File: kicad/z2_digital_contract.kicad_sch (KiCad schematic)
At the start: 0 parts

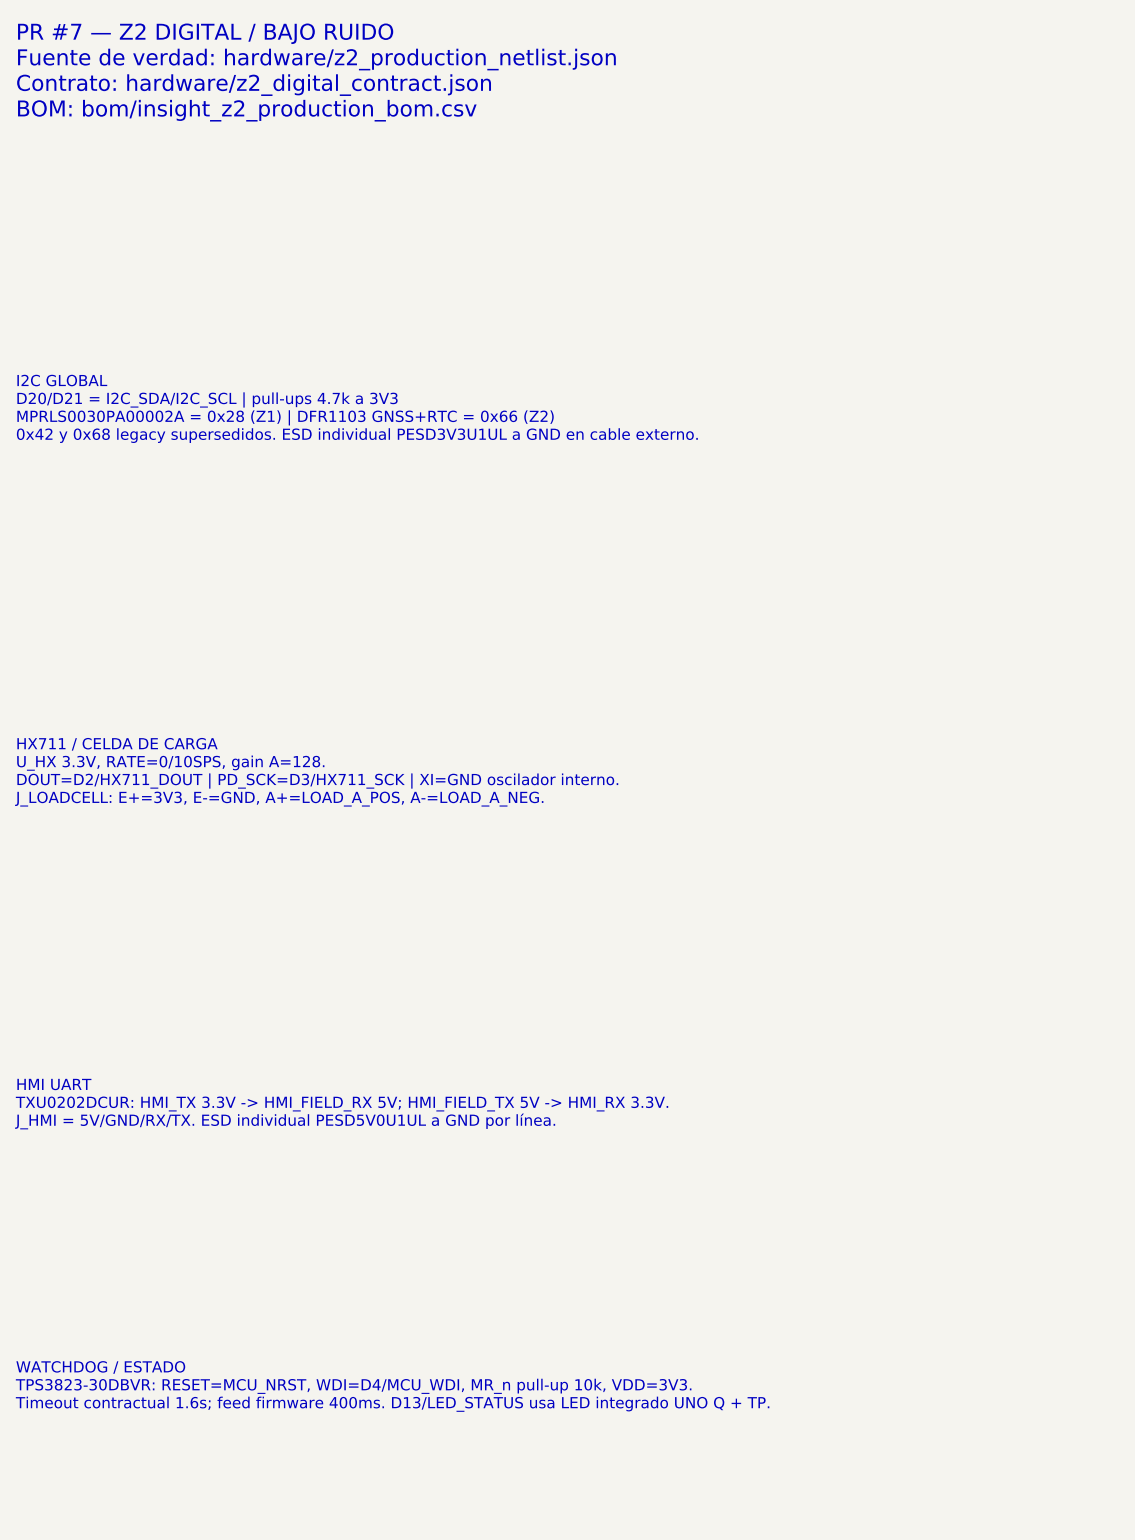
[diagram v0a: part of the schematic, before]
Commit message: potencia: congelar arquitectura Fase 3 y frontera UNO Q (#9)
Congela el power tree del shield sobre 12V→VIN UNO Q, separa rails locales 5V/3V3, selecciona eFuse/buck/LDO, formaliza GitHub oficial Arduino como fuente primaria y mantiene Z1/Z2/compliance coherentes.
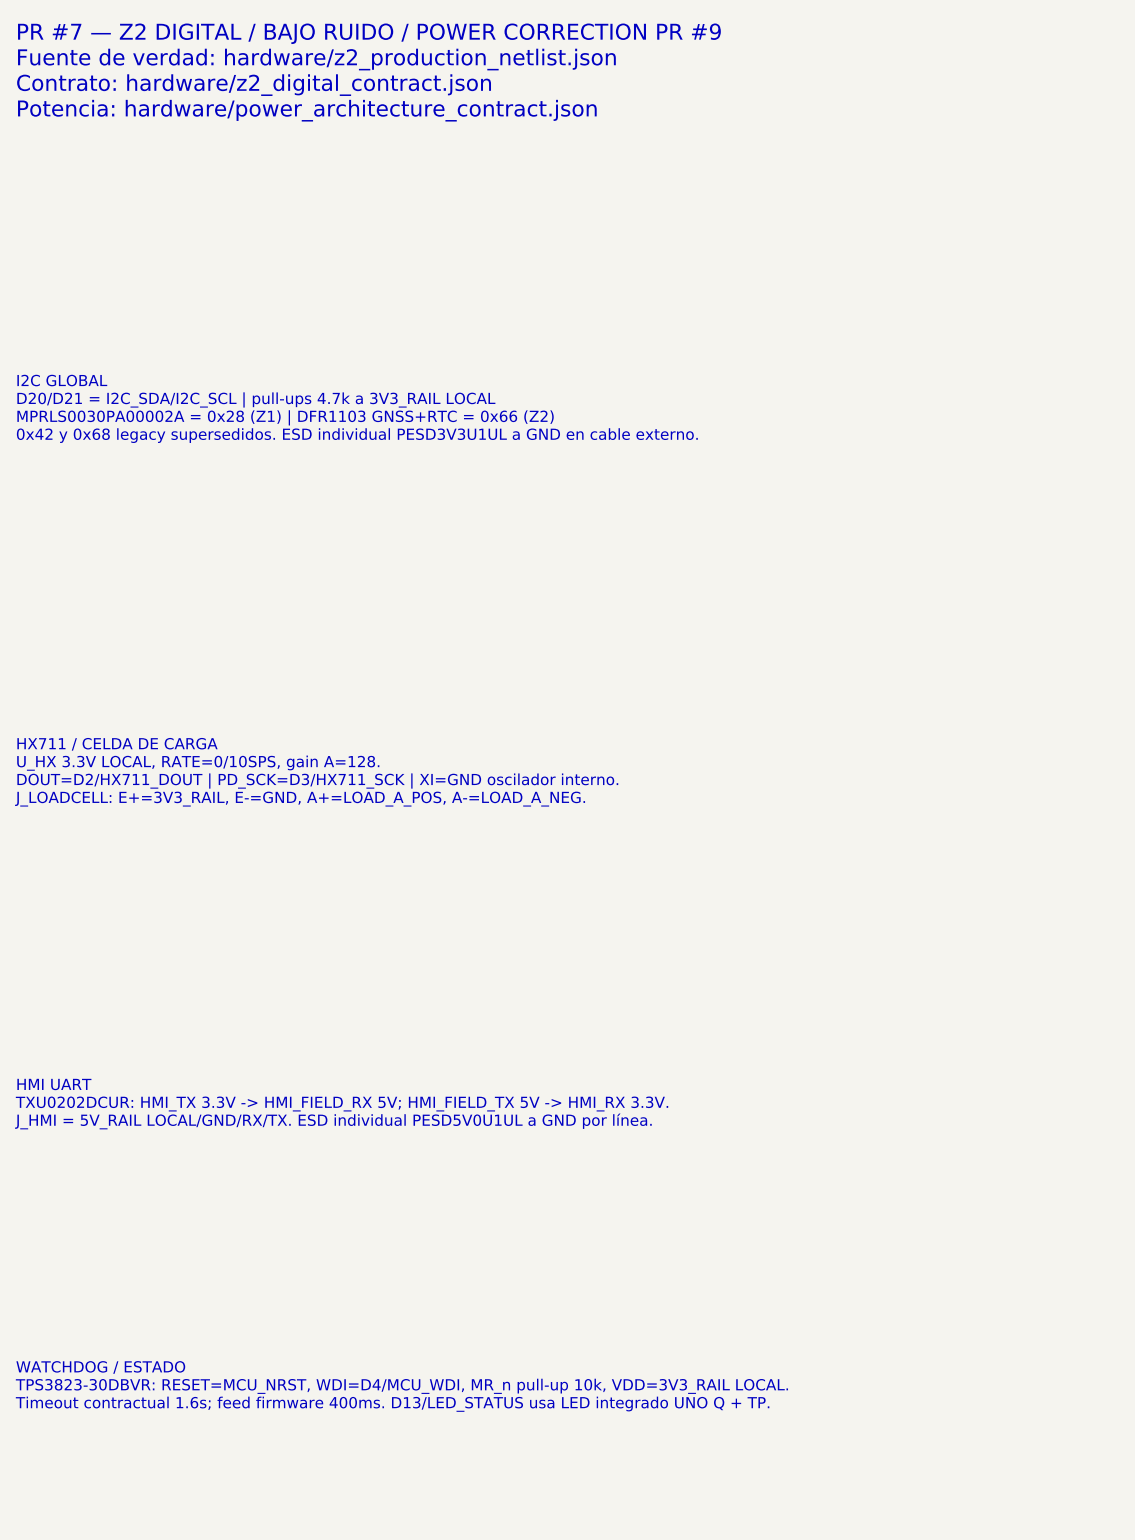
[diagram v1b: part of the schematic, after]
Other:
- note added: "HMI UART TXU0202DCUR: HMI_TX 3.3V -> HMI_FIELD_RX 5V; HMI_FIELD_TX 5V -> HMI_RX 3.3V. J_HMI = 5V_RAIL LOCAL/GND/RX/TX. ESD individual PESD5V0U1UL a GND por línea."
- note added: "HX711 / CELDA DE CARGA U_HX 3.3V LOCAL, RATE=0/10SPS, gain A=128. DOUT=D2/HX711_DOUT | PD_SCK=D3/HX711_SCK | XI=GND oscilador interno. J_LOADCELL: E+=3V3_RAIL, E-=GND, A+=LOAD_A_POS, A-=LOAD_A_NEG."
- note added: "I2C GLOBAL D20/D21 = I2C_SDA/I2C_SCL | pull-ups 4.7k a 3V3_RAIL LOCAL MPRLS0030PA00002A = 0x28 (Z1) | DFR1103 GNSS+RTC = 0x66 (Z2) 0x42 y 0x68 legacy supersedidos. ESD individual PESD3V3U1UL a GND en cable externo."
- note added: "PR #7 — Z2 DIGITAL / BAJO RUIDO / POWER CORRECTION PR #9 Fuente de verdad: hardware/z2_production_netlist.json Contrato: hardware/z2_digital_contract.json Potencia: hardware/power_architecture_contract.json"
- note added: "WATCHDOG / ESTADO TPS3823-30DBVR: RESET=MCU_NRST, WDI=D4/MCU_WDI, MR_n pull-up 10k, VDD=3V3_RAIL LOCAL. Timeout contractual 1.6s; feed firmware 400ms. D13/LED_STATUS usa LED integrado UNO Q + TP."
- note removed: "HMI UART TXU0202DCUR: HMI_TX 3.3V -> HMI_FIELD_RX 5V; HMI_FIELD_TX 5V -> HMI_RX 3.3V. J_HMI = 5V/GND/RX/TX. ESD individual PESD5V0U1UL a GND por línea."
- note removed: "HX711 / CELDA DE CARGA U_HX 3.3V, RATE=0/10SPS, gain A=128. DOUT=D2/HX711_DOUT | PD_SCK=D3/HX711_SCK | XI=GND oscilador interno. J_LOADCELL: E+=3V3, E-=GND, A+=LOAD_A_POS, A-=LOAD_A_NEG."
- note removed: "I2C GLOBAL D20/D21 = I2C_SDA/I2C_SCL | pull-ups 4.7k a 3V3 MPRLS0030PA00002A = 0x28 (Z1) | DFR1103 GNSS+RTC = 0x66 (Z2) 0x42 y 0x68 legacy supersedidos. ESD individual PESD3V3U1UL a GND en cable externo."
- note removed: "PR #7 — Z2 DIGITAL / BAJO RUIDO Fuente de verdad: hardware/z2_production_netlist.json Contrato: hardware/z2_digital_contract.json BOM: bom/insight_z2_production_bom.csv"
- note removed: "WATCHDOG / ESTADO TPS3823-30DBVR: RESET=MCU_NRST, WDI=D4/MCU_WDI, MR_n pull-up 10k, VDD=3V3. Timeout contractual 1.6s; feed firmware 400ms. D13/LED_STATUS usa LED integrado UNO Q + TP."
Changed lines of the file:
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@@
   (version 20250114)
   (generator "nfb_pr7_contract")
-  (generator_version "1.0")
+  (generator_version "1.1")
   (paper "A3")
   (title_block
     (title "NFB Insight PCBA v2 — Z2 Digital / Bajo Ruido")
     (date "2026-08-11")
-    (rev "0.7.0")
+    (rev "0.9.0")
     (company "Cafelium SRL / Nebula Ecosystem")
-    (comment 1 "PR #7 — contrato Z2 gobernado por hardware/z2_production_netlist.json")
+    (comment 1 "PR #7 Z2 preservado; frontera de potencia corregida por PR #9")
     (comment 2 "DFR1103 0x66 | HX711 | TXU0202DCUR | TPS3823-30DBVR")
-    (comment 3 "Placement/routing fuera de alcance")
-    (comment 4 "Integración jerárquica Z1+Z2 posterior")
+    (comment 3 "5V_RAIL/3V3_RAIL son locales al shield; no J_UNOQ.4/.5")
+    (comment 4 "Placement/routing fuera de alcance")
   )
-  (text "PR #7 — Z2 DIGITAL / BAJO RUIDO\nFuente de verdad: hardware/z2_production_netlist.json\nContrato: hardware/z2_digital_contract.json\nBOM: bom/insight_z2_production_bom.csv"
+  (text "PR #7 — Z2 DIGITAL / BAJO RUIDO / POWER CORRECTION PR #9\nFuente de verdad: hardware/z2_production_netlist.json\nContrato: hardware/z2_digital_contract.json\nPotencia: hardware/power_architecture_contract.json"
     (exclude_from_sim no)
     (at 38.1 35.56 0)
     (effects (font (size 2 2)) (justify left bottom))
   )
-  (text "I2C GLOBAL\nD20/D21 = I2C_SDA/I2C_SCL | pull-ups 4.7k a 3V3\nMPRLS0030PA00002A = 0x28 (Z1) | DFR1103 GNSS+RTC = 0x66 (Z2)\n0x42 y 0x68 legacy supersedidos. ESD individual PESD3V3U1UL a GND en cable externo."
+  (text "I2C GLOBAL\nD20/D21 = I2C_SDA/I2C_SCL | pull-ups 4.7k a 3V3_RAIL LOCAL\nMPRLS0030PA00002A = 0x28 (Z1) | DFR1103 GNSS+RTC = 0x66 (Z2)\n0x42 y 0x68 legacy supersedidos. ESD individual PESD3V3U1UL a GND en cable externo."
     (exclude_from_sim no)
     (at 38.1 76.2 0)
     (effects (font (size 1.4 1.4)) (justify left bottom))
   )
-  (text "HX711 / CELDA DE CARGA\nU_HX 3.3V, RATE=0/10SPS, gain A=128.\nDOUT=D2/HX711_DOUT | PD_SCK=D3/HX711_SCK | XI=GND oscilador interno.\nJ_LOADCELL: E+=3V3, E-=GND, A+=LOAD_A_POS, A-=LOAD_A_NEG."
+  (text "HX711 / CELDA DE CARGA\nU_HX 3.3V LOCAL, RATE=0/10SPS, gain A=128.\nDOUT=D2/HX711_DOUT | PD_SCK=D3/HX711_SCK | XI=GND oscilador interno.\nJ_LOADCELL: E+=3V3_RAIL, E-=GND, A+=LOAD_A_POS, A-=LOAD_A_NEG."
     (exclude_from_sim no)
     (at 38.1 121.92 0)
     (effects (font (size 1.4 1.4)) (justify left bottom))
   )
-  (text "HMI UART\nTXU0202DCUR: HMI_TX 3.3V -> HMI_FIELD_RX 5V; HMI_FIELD_TX 5V -> HMI_RX 3.3V.\nJ_HMI = 5V/GND/RX/TX. ESD individual PESD5V0U1UL a GND por línea."
+  (text "HMI UART\nTXU0202DCUR: HMI_TX 3.3V -> HMI_FIELD_RX 5V; HMI_FIELD_TX 5V -> HMI_RX 3.3V.\nJ_HMI = 5V_RAIL LOCAL/GND/RX/TX. ESD individual PESD5V0U1UL a GND por línea."
     (exclude_from_sim no)
     (at 38.1 162.56 0)
     (effects (font (size 1.4 1.4)) (justify left bottom))
   )
-  (text "WATCHDOG / ESTADO\nTPS3823-30DBVR: RESET=MCU_NRST, WDI=D4/MCU_WDI, MR_n pull-up 10k, VDD=3V3.\nTimeout contractual 1.6s; feed firmware 400ms. D13/LED_STATUS usa LED integrado UNO Q + TP."
+  (text "WATCHDOG / ESTADO\nTPS3823-30DBVR: RESET=MCU_NRST, WDI=D4/MCU_WDI, MR_n pull-up 10k, VDD=3V3_RAIL LOCAL.\nTimeout contractual 1.6s; feed firmware 400ms. D13/LED_STATUS usa LED integrado UNO Q + TP."
     (exclude_from_sim no)
     (at 38.1 198.12 0)
